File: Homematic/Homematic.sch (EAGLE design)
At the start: 28 parts, among them IC1 3.3V, IC2 3.3V, P1 DF11-06-2DS, Q1 BS170

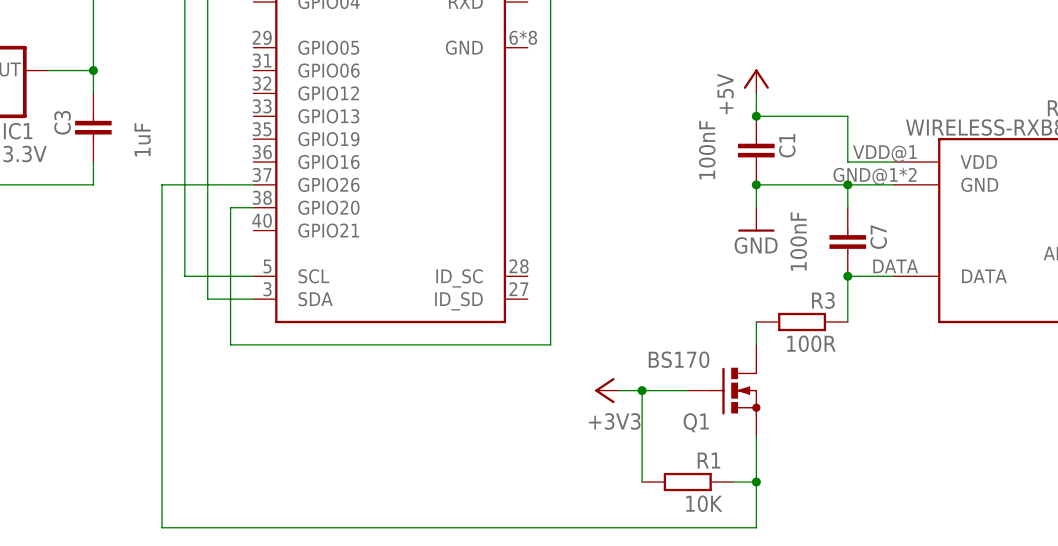
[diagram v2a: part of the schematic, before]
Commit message: Fix low pass filter. Move suppressor diode. Move documentation from top to bottom layer.
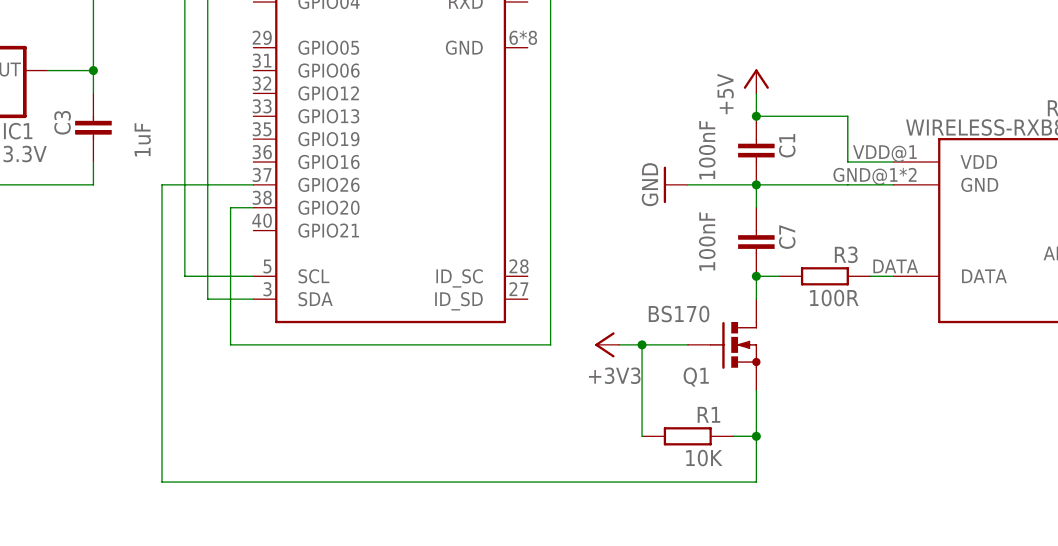
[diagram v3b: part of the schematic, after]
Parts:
- R3: device rcl:R-EU_0204/5 -> rcl:R-EU_0204/2V
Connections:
- net N$11: now also C7.2
- net N$3: no longer C7.2
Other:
- moved on the sheet: C7, Q1, R1, R3
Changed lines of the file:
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@@
 <part name="+3V1" library="supply1" deviceset="+3V3" device=""/>
 <part name="+3V2" library="supply1" deviceset="+3V3" device=""/>
-<part name="R3" library="rcl" deviceset="R-EU_" device="0204/5" value="100R">
+<part name="R3" library="rcl" deviceset="R-EU_" device="0204/2V" value="100R">
 <attribute name="MF" value=""/>
 <attribute name="MPN" value=""/>
@@
 </instance>
 <instance part="GND2" gate="1" x="256.54" y="27.94"/>
-<instance part="Q1" gate="1" x="198.12" y="22.86" smashed="yes">
-<attribute name="OC_FARNELL" x="198.12" y="22.86" size="1.778" layer="96" rot="R270" display="off"/>
-<attribute name="MF" x="198.12" y="22.86" size="1.778" layer="96" rot="R270" display="off"/>
-<attribute name="MPN" x="198.12" y="22.86" size="1.778" layer="96" rot="R270" display="off"/>
-<attribute name="NAME" x="195.58" y="20.32" size="1.778" layer="95" align="top-right"/>
-<attribute name="VALUE" x="195.58" y="25.4" size="1.778" layer="96" align="bottom-right"/>
-</instance>
-<instance part="R1" gate="G$1" x="193.04" y="12.7" rot="MR0">
-<attribute name="OC_FARNELL" x="193.04" y="12.7" size="1.778" layer="96" rot="MR270" display="off"/>
-<attribute name="MF" x="193.04" y="12.7" size="1.778" layer="96" rot="MR270" display="off"/>
-<attribute name="MPN" x="193.04" y="12.7" size="1.778" layer="96" rot="MR270" display="off"/>
+<instance part="Q1" gate="1" x="198.12" y="27.94" smashed="yes">
+<attribute name="OC_FARNELL" x="198.12" y="27.94" size="1.778" layer="96" rot="R270" display="off"/>
+<attribute name="MF" x="198.12" y="27.94" size="1.778" layer="96" rot="R270" display="off"/>
+<attribute name="MPN" x="198.12" y="27.94" size="1.778" layer="96" rot="R270" display="off"/>
+<attribute name="NAME" x="195.58" y="25.4" size="1.778" layer="95" align="top-right"/>
+<attribute name="VALUE" x="195.58" y="30.48" size="1.778" layer="96" align="bottom-right"/>
+</instance>
+<instance part="R1" gate="G$1" x="193.04" y="17.78" rot="MR0">
+<attribute name="OC_FARNELL" x="193.04" y="17.78" size="1.778" layer="96" rot="MR270" display="off"/>
+<attribute name="MF" x="193.04" y="17.78" size="1.778" layer="96" rot="MR270" display="off"/>
+<attribute name="MPN" x="193.04" y="17.78" size="1.778" layer="96" rot="MR270" display="off"/>
 </instance>
 <instance part="MP1584-2" gate="G$1" x="50.8" y="93.98"/>
@@
 <attribute name="MPN" x="198.12" y="91.44" size="1.778" layer="96" rot="MR0" display="off"/>
 </instance>
-<instance part="GND6" gate="1" x="200.66" y="40.64"/>
+<instance part="GND6" gate="1" x="190.5" y="45.72" rot="R270"/>
 <instance part="C1" gate="G$1" x="200.66" y="50.8" smashed="yes" rot="MR0">
 <attribute name="NAME" x="203.2" y="48.641" size="1.778" layer="95" rot="MR90"/>
@@
 <instance part="P+4" gate="1" x="200.66" y="58.42"/>
 <instance part="+3V1" gate="G$1" x="213.36" y="129.54"/>
-<instance part="+3V2" gate="G$1" x="182.88" y="22.86" rot="R90"/>
-<instance part="R3" gate="G$1" x="205.74" y="30.48" rot="MR0">
-<attribute name="OC_FARNELL" x="205.74" y="30.48" size="1.778" layer="96" rot="MR270" display="off"/>
-<attribute name="MF" x="205.74" y="30.48" size="1.778" layer="96" rot="MR270" display="off"/>
-<attribute name="MPN" x="205.74" y="30.48" size="1.778" layer="96" rot="MR270" display="off"/>
-</instance>
-<instance part="C7" gate="G$1" x="210.82" y="40.64" smashed="yes" rot="MR0">
-<attribute name="NAME" x="213.36" y="38.481" size="1.778" layer="95" rot="MR90"/>
-<attribute name="VALUE" x="204.47" y="35.941" size="1.778" layer="96" rot="MR90"/>
+<instance part="+3V2" gate="G$1" x="182.88" y="27.94" rot="R90"/>
+<instance part="R3" gate="G$1" x="208.28" y="35.56" rot="MR0">
+<attribute name="OC_FARNELL" x="208.28" y="35.56" size="1.778" layer="96" rot="MR270" display="off"/>
+<attribute name="MF" x="208.28" y="35.56" size="1.778" layer="96" rot="MR270" display="off"/>
+<attribute name="MPN" x="208.28" y="35.56" size="1.778" layer="96" rot="MR270" display="off"/>
+</instance>
+<instance part="C7" gate="G$1" x="200.66" y="40.64" smashed="yes" rot="MR0">
+<attribute name="NAME" x="203.2" y="38.481" size="1.778" layer="95" rot="MR90"/>
+<attribute name="VALUE" x="194.31" y="35.941" size="1.778" layer="96" rot="MR90"/>
 </instance>
 </instances>
@@
 <wire x1="215.9" y1="45.72" x2="210.82" y2="45.72" width="0.1524" layer="91"/>
 <wire x1="210.82" y1="45.72" x2="200.66" y2="45.72" width="0.1524" layer="91"/>
-<wire x1="200.66" y1="45.72" x2="200.66" y2="43.18" width="0.1524" layer="91"/>
+<wire x1="200.66" y1="45.72" x2="193.04" y2="45.72" width="0.1524" layer="91"/>
 <pinref part="C1" gate="G$1" pin="2"/>
 <junction x="200.66" y="45.72"/>
 <pinref part="C7" gate="G$1" pin="1"/>
-<wire x1="210.82" y1="43.18" x2="210.82" y2="45.72" width="0.1524" layer="91"/>
-<junction x="210.82" y="45.72"/>
-</segment>
-</net>
-<net name="N$3" class="0">
-<segment>
-<wire x1="210.82" y1="35.56" x2="215.9" y2="35.56" width="0.1524" layer="91"/>
-<pinref part="RXB8" gate="G$1" pin="DATA"/>
-<pinref part="C7" gate="G$1" pin="2"/>
-<pinref part="R3" gate="G$1" pin="1"/>
-<wire x1="210.82" y1="35.56" x2="210.82" y2="30.48" width="0.1524" layer="91"/>
-<junction x="210.82" y="35.56"/>
+<wire x1="200.66" y1="43.18" x2="200.66" y2="45.72" width="0.1524" layer="91"/>
 </segment>
 </net>
@@
 <pinref part="R1" gate="G$1" pin="2"/>
 <pinref part="Q1" gate="1" pin="G"/>
-<wire x1="193.04" y1="22.86" x2="187.96" y2="22.86" width="0.1524" layer="91"/>
-<wire x1="187.96" y1="22.86" x2="187.96" y2="12.7" width="0.1524" layer="91"/>
+<wire x1="193.04" y1="27.94" x2="187.96" y2="27.94" width="0.1524" layer="91"/>
+<wire x1="187.96" y1="27.94" x2="187.96" y2="17.78" width="0.1524" layer="91"/>
 <pinref part="+3V2" gate="G$1" pin="+3V3"/>
-<wire x1="187.96" y1="22.86" x2="185.42" y2="22.86" width="0.1524" layer="91"/>
-<junction x="187.96" y="22.86"/>
+<wire x1="187.96" y1="27.94" x2="185.42" y2="27.94" width="0.1524" layer="91"/>
+<junction x="187.96" y="27.94"/>
 </segment>
 </net>
@@
 </segment>
 </net>
-<net name="N$11" class="0">
-<segment>
-<pinref part="Q1" gate="1" pin="D"/>
-<pinref part="R3" gate="G$1" pin="2"/>
-<wire x1="200.66" y1="27.94" x2="200.66" y2="30.48" width="0.1524" layer="91"/>
-</segment>
-</net>
 <net name="N$10" class="0">
 <segment>
-<wire x1="134.62" y1="7.62" x2="134.62" y2="45.72" width="0.1524" layer="91"/>
+<wire x1="134.62" y1="12.7" x2="134.62" y2="45.72" width="0.1524" layer="91"/>
 <pinref part="RPI" gate="G$1" pin="GPIO26"/>
 <wire x1="134.62" y1="45.72" x2="144.78" y2="45.72" width="0.1524" layer="91"/>
 <pinref part="Q1" gate="1" pin="S"/>
+<wire x1="200.66" y1="22.86" x2="200.66" y2="17.78" width="0.1524" layer="91"/>
+<pinref part="R1" gate="G$1" pin="1"/>
+<wire x1="198.12" y1="17.78" x2="200.66" y2="17.78" width="0.1524" layer="91"/>
+<junction x="200.66" y="17.78"/>
 <wire x1="200.66" y1="17.78" x2="200.66" y2="12.7" width="0.1524" layer="91"/>
-<pinref part="R1" gate="G$1" pin="1"/>
-<wire x1="198.12" y1="12.7" x2="200.66" y2="12.7" width="0.1524" layer="91"/>
-<junction x="200.66" y="12.7"/>
-<wire x1="200.66" y1="12.7" x2="200.66" y2="7.62" width="0.1524" layer="91"/>
-<wire x1="134.62" y1="7.62" x2="200.66" y2="7.62" width="0.1524" layer="91"/>
-</segment>
-</net>
+<wire x1="134.62" y1="12.7" x2="200.66" y2="12.7" width="0.1524" layer="91"/>
+</segment>
+</net>
+<net name="N$3" class="0">
+<segment>
+<pinref part="RXB8" gate="G$1" pin="DATA"/>
+<pinref part="R3" gate="G$1" pin="1"/>
+<wire x1="215.9" y1="35.56" x2="213.36" y2="35.56" width="0.1524" layer="91"/>
+</segment>
+</net>
+<net name="N$11" class="0">
+<segment>
+<pinref part="R3" gate="G$1" pin="2"/>
+<pinref part="C7" gate="G$1" pin="2"/>
+<wire x1="203.2" y1="35.56" x2="200.66" y2="35.56" width="0.1524" layer="91"/>
+<pinref part="Q1" gate="1" pin="D"/>
+<wire x1="200.66" y1="35.56" x2="200.66" y2="33.02" width="0.1524" layer="91"/>
+<junction x="200.66" y="35.56"/>
+</segment>
+</net>

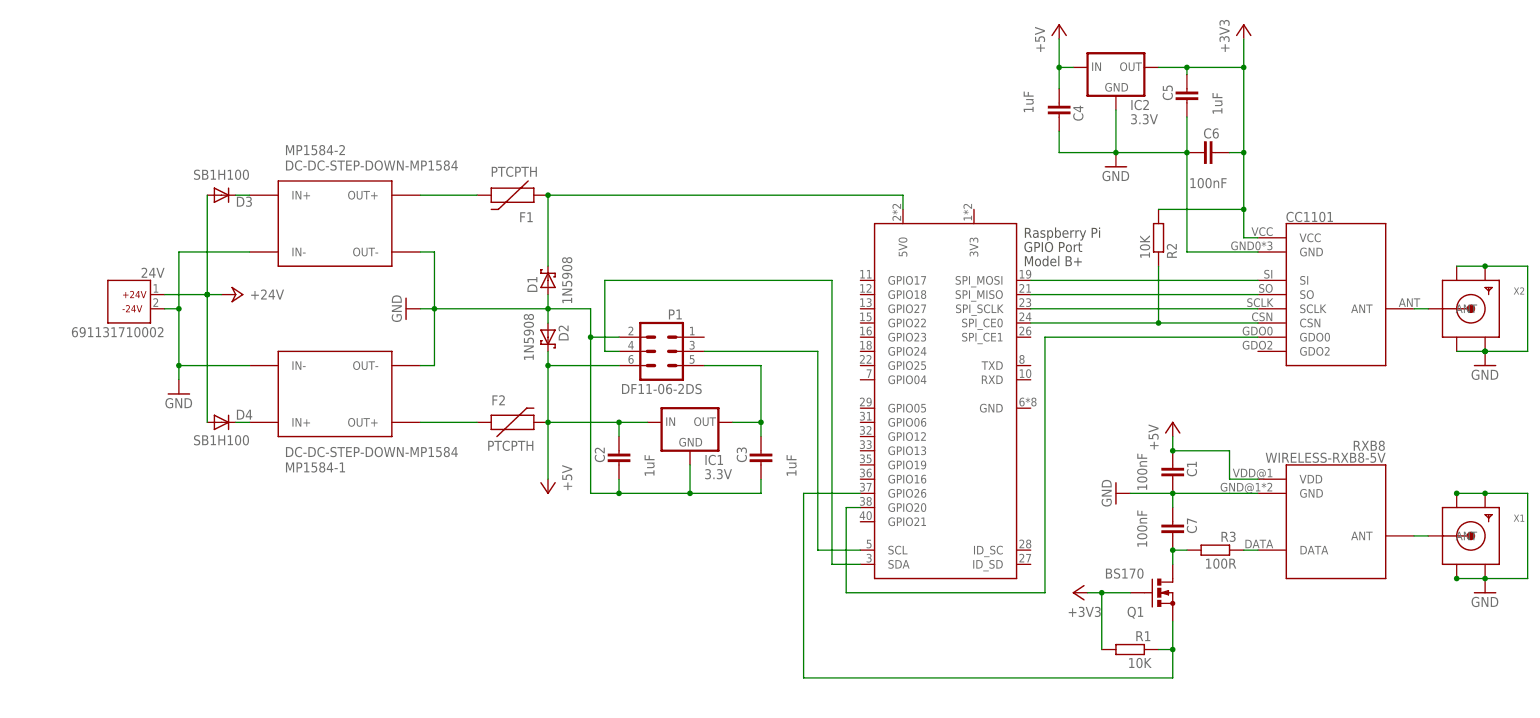
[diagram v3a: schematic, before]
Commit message: Replace package for CC1101 receiver
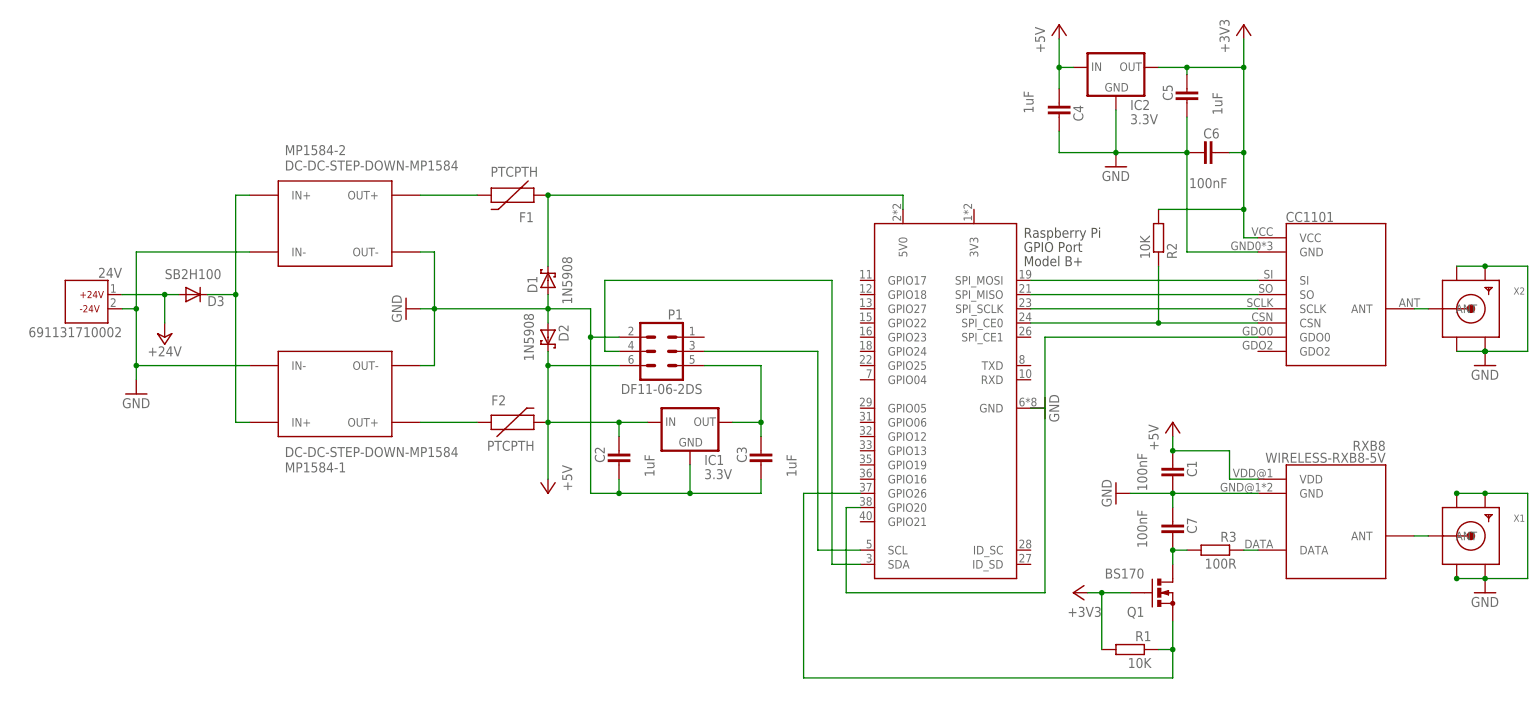
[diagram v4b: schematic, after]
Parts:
- removed D4: SB1H100, diode:DIODE-DO41-7.6
- CC1101: value CC1101 -> CC1101SMD; device modules:CC1101 -> modules:CC1101SMD
- D3: value SB1H100 -> SB2H100
- R2: device rcl:R-EU_0204/2V -> rcl:R-EU_0204/7
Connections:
- removed net N$9: D4.C, MP1584-1.IN+
- net +24V: no longer D4.A
- net GND: now also RPI.GND
- net N$7: now also MP1584-1.IN+
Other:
- moved on the sheet: 24V, D3

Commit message: Change some routes
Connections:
- net N$10: now also RPI.GPIO21; no longer RPI.GPIO26
- net N$19: now also RPI.GPIO12; no longer RPI.GPIO20
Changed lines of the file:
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@@
 <attribute name="VALUE" x="194.31" y="35.941" size="1.778" layer="96" rot="MR90"/>
 </instance>
-<instance part="GND7" gate="1" x="177.8" y="60.96" rot="R90"/>
+<instance part="GND7" gate="1" x="177.8" y="58.42"/>
 </instances>
 <busses>
@@
 <net name="N$19" class="0">
 <segment>
-<wire x1="142.24" y1="27.94" x2="177.8" y2="27.94" width="0.1524" layer="91"/>
-<wire x1="177.8" y1="27.94" x2="177.8" y2="73.66" width="0.1524" layer="91"/>
+<wire x1="142.24" y1="27.94" x2="180.34" y2="27.94" width="0.1524" layer="91"/>
+<wire x1="180.34" y1="27.94" x2="180.34" y2="73.66" width="0.1524" layer="91"/>
 <pinref part="CC1101" gate="G$1" pin="GDO0"/>
-<wire x1="177.8" y1="73.66" x2="215.9" y2="73.66" width="0.1524" layer="91"/>
-<pinref part="RPI" gate="G$1" pin="GPIO20"/>
-<wire x1="142.24" y1="27.94" x2="142.24" y2="43.18" width="0.1524" layer="91"/>
-<wire x1="142.24" y1="43.18" x2="144.78" y2="43.18" width="0.1524" layer="91"/>
+<wire x1="180.34" y1="73.66" x2="215.9" y2="73.66" width="0.1524" layer="91"/>
+<wire x1="142.24" y1="27.94" x2="142.24" y2="55.88" width="0.1524" layer="91"/>
+<pinref part="RPI" gate="G$1" pin="GPIO12"/>
+<wire x1="142.24" y1="55.88" x2="144.78" y2="55.88" width="0.1524" layer="91"/>
 </segment>
 </net>
@@
 <net name="N$10" class="0">
 <segment>
-<wire x1="134.62" y1="12.7" x2="134.62" y2="45.72" width="0.1524" layer="91"/>
-<pinref part="RPI" gate="G$1" pin="GPIO26"/>
-<wire x1="134.62" y1="45.72" x2="144.78" y2="45.72" width="0.1524" layer="91"/>
+<wire x1="134.62" y1="12.7" x2="134.62" y2="40.64" width="0.1524" layer="91"/>
 <pinref part="Q1" gate="1" pin="S"/>
 <wire x1="200.66" y1="22.86" x2="200.66" y2="17.78" width="0.1524" layer="91"/>
@@
 <wire x1="200.66" y1="17.78" x2="200.66" y2="12.7" width="0.1524" layer="91"/>
 <wire x1="134.62" y1="12.7" x2="200.66" y2="12.7" width="0.1524" layer="91"/>
-</segment>
-</net>
+<pinref part="RPI" gate="G$1" pin="GPIO21"/>
+<wire x1="134.62" y1="40.64" x2="144.78" y2="40.64" width="0.1524" layer="91"/>
+</segment>
+</net>
